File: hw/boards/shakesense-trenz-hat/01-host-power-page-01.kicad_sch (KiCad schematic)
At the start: 9 parts, among them J1 Raspberry Pi 40-pin, U1 24LC32A

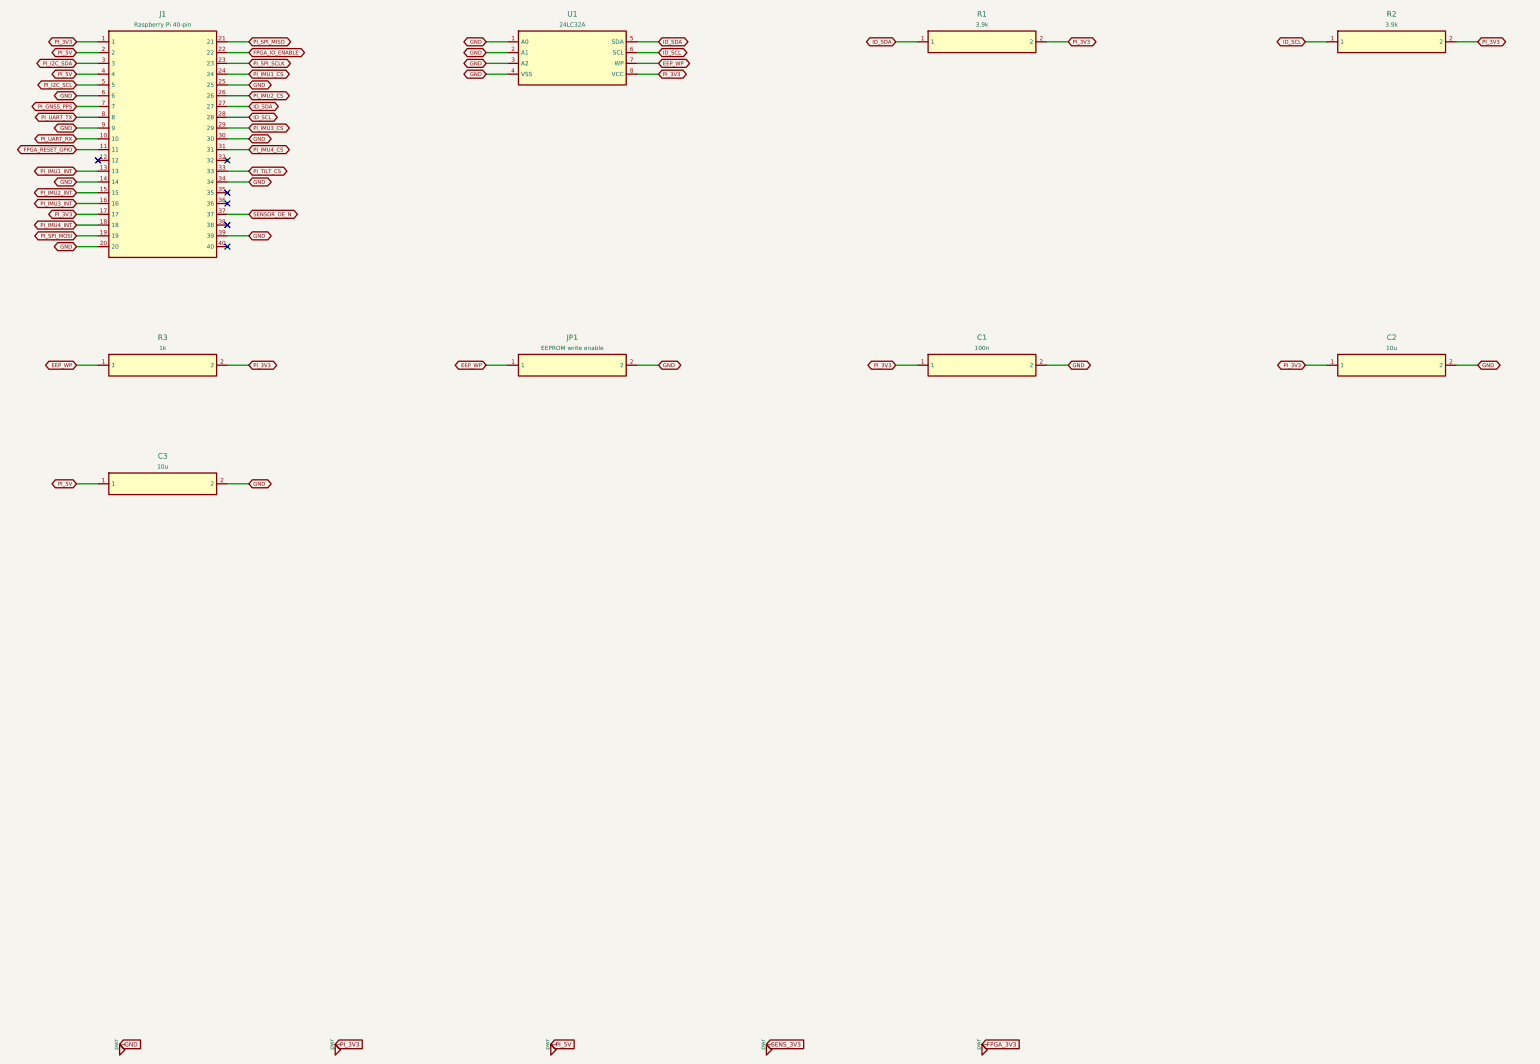
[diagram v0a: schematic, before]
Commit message: Expose Trenz GPIOs on the Pi-outline HDI sensor HAT
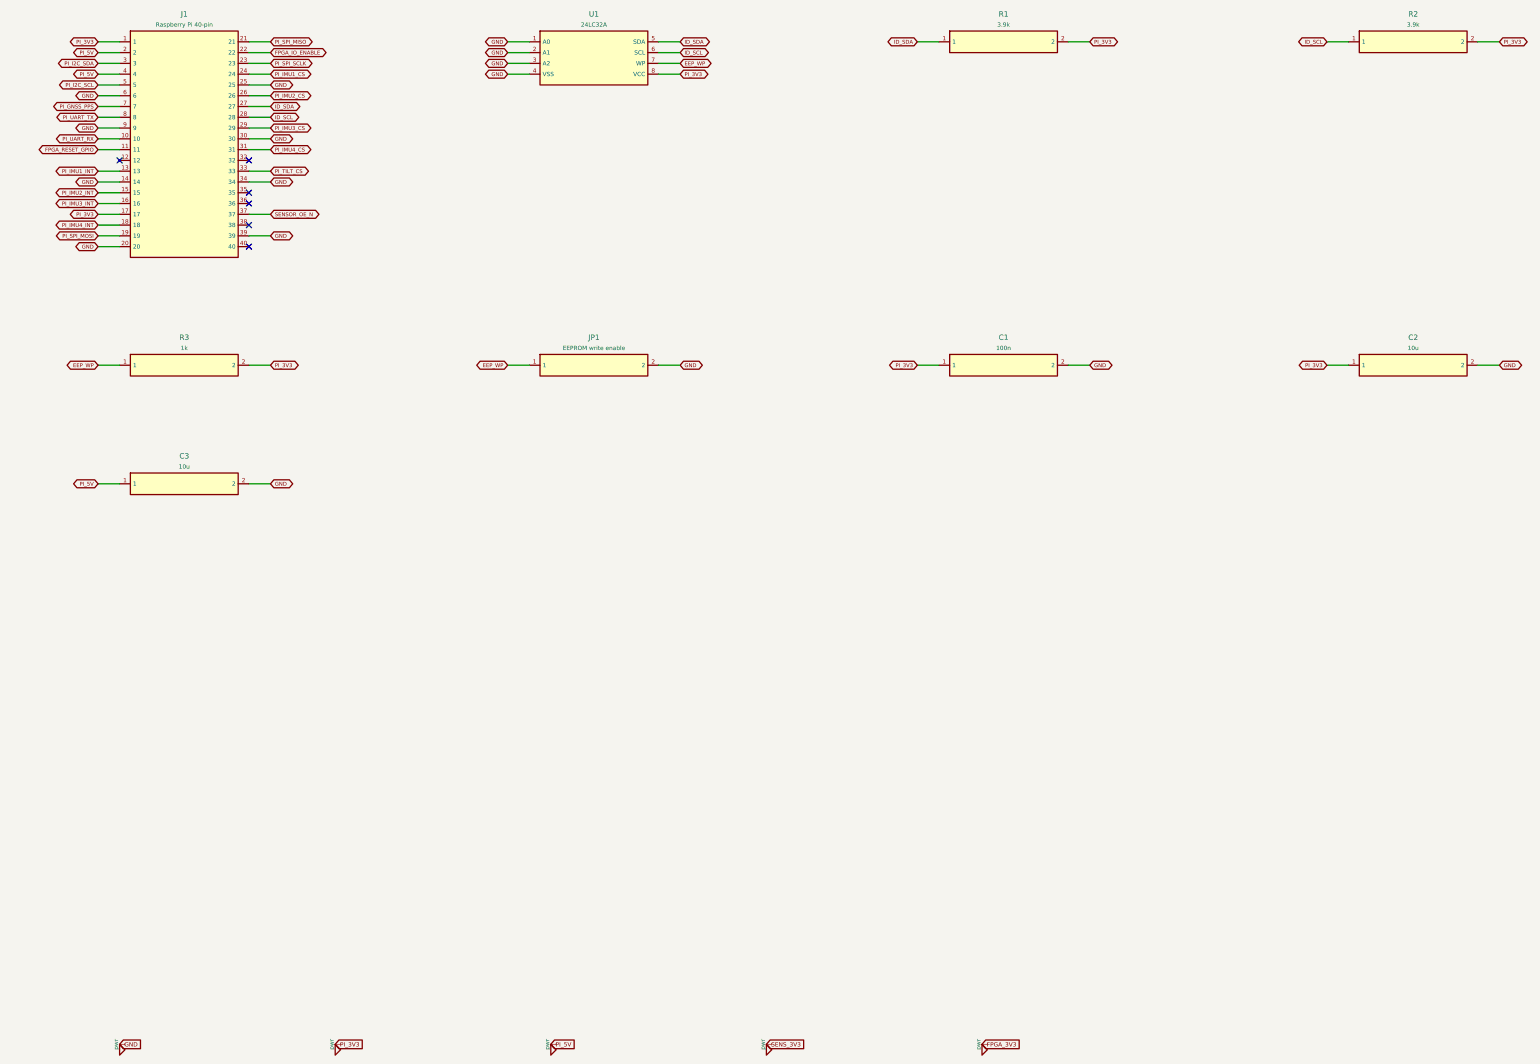
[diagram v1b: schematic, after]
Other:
- title: shakesense-trenz-hat / 01-host-power-page-01 -> ShakeSense T1 / 01-host-power-page-01
- moved on the sheet: C1, C2, C3, J1, JP1, R1, R2, R3, U1

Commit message: Replace T1 GNSS with single Racotech geophone input
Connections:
- net PI_GNSS_PPS renamed PI_GEO_DRDY_N
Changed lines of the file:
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@@
-(kicad_sch (version 20230121) (generator eeschema) (paper "A3") (title_block (title "ShakeSense T1 / 01-host-power-page-01") (date "2026-09-24") (rev "T1-GPIO"))
+(kicad_sch (version 20230121) (generator eeschema) (paper "A3") (title_block (title "ShakeSense T1 / 01-host-power-page-01") (date "2026-09-24") (rev "T1-GEO"))
 (symbol (lib_id "ShakeSense:Part_J1") (at 50.8 62.230000000000004 0) (unit 1) (in_bom yes) (on_board yes) (dnp no)
               (property "Reference" "J1" (at 50.8 31.560000000000002 0) (effects (font (size 1.27 1.27))))
@@
 (global_label "GND" (shape bidirectional) (at 30.48 50.8 180) (effects (font (size 0.9 0.9)) (justify right)))
 (wire (pts (xy 35.56 53.34) (xy 30.48 53.34)) (stroke (width 0) (type default)))
-(global_label "PI_GNSS_PPS" (shape bidirectional) (at 30.48 53.34 180) (effects (font (size 0.9 0.9)) (justify right)))
+(global_label "PI_GEO_DRDY_N" (shape bidirectional) (at 30.48 53.34 180) (effects (font (size 0.9 0.9)) (justify right)))
 (wire (pts (xy 35.56 55.88) (xy 30.48 55.88)) (stroke (width 0) (type default)))
 (global_label "PI_UART_TX" (shape bidirectional) (at 30.48 55.88 180) (effects (font (size 0.9 0.9)) (justify right)))
@@
 (symbol (lib_id "ShakeSense:PWR_FLAG") (at 238.76 274.32 0) (unit 1) (in_bom no) (on_board no) (property "Reference" "#FLG05" (at 238.76 274.32 0) (effects (font (size 1 1)) hide)) (property "Value" "PWR_FLAG" (at 238.76 274.32 0) (effects (font (size 1 1)) hide)) (instances (project "shakesense-trenz-hat" (path "/4ffaaa5d-c728-540d-9f0f-f1cafbdbe36e/94e4fefa-b04f-5cb8-86ce-dd5f9a42bc5a" (reference "#FLG05") (unit 1)))))
 (global_label "FPGA_3V3" (shape input) (at 238.76 274.32 0) (effects (font (size 1.0 1.0)) (justify left)))
+(symbol (lib_id "ShakeSense:PWR_FLAG") (at 289.56 274.32 0) (unit 1) (in_bom no) (on_board no) (property "Reference" "#FLG06" (at 289.56 274.32 0) (effects (font (size 1 1)) hide)) (property "Value" "PWR_FLAG" (at 289.56 274.32 0) (effects (font (size 1 1)) hide)) (instances (project "shakesense-trenz-hat" (path "/4ffaaa5d-c728-540d-9f0f-f1cafbdbe36e/94e4fefa-b04f-5cb8-86ce-dd5f9a42bc5a" (reference "#FLG06") (unit 1)))))
+(global_label "GEO_AVDD" (shape input) (at 289.56 274.32 0) (effects (font (size 1.0 1.0)) (justify left)))
 )

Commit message: Implement internal Pi FPGA link and remove ribbon expansion
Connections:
- net PI_LINK_CS_N: now reaches J1.12
- net PI_LINK_DQ3: now reaches J1.32
- net PI_LINK_DQ1: now reaches J1.35
- net PI_LINK_DQ2: now reaches J1.36
- net PI_LINK_DQ0: now reaches J1.38
- net PI_LINK_SCLK: now reaches J1.40
- no-connect marks 6 -> 0
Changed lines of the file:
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@@
 (wire (pts (xy 35.56 63.5) (xy 30.48 63.5)) (stroke (width 0) (type default)))
 (global_label "FPGA_RESET_GPIO" (shape bidirectional) (at 30.48 63.5 180) (effects (font (size 0.9 0.9)) (justify right)))
-(no_connect (at 35.56 66.04))
+(wire (pts (xy 35.56 66.04) (xy 30.48 66.04)) (stroke (width 0) (type default)))
+(global_label "PI_LINK_CS_N" (shape bidirectional) (at 30.48 66.04 180) (effects (font (size 0.9 0.9)) (justify right)))
 (wire (pts (xy 35.56 68.58) (xy 30.48 68.58)) (stroke (width 0) (type default)))
 (global_label "PI_IMU1_INT" (shape bidirectional) (at 30.48 68.58 180) (effects (font (size 0.9 0.9)) (justify right)))
@@
 (wire (pts (xy 66.04 63.5) (xy 71.12 63.5)) (stroke (width 0) (type default)))
 (global_label "PI_IMU4_CS" (shape bidirectional) (at 71.12 63.5 0) (effects (font (size 0.9 0.9)) (justify left)))
-(no_connect (at 66.04 66.04))
+(wire (pts (xy 66.04 66.04) (xy 71.12 66.04)) (stroke (width 0) (type default)))
+(global_label "PI_LINK_DQ3" (shape bidirectional) (at 71.12 66.04 0) (effects (font (size 0.9 0.9)) (justify left)))
 (wire (pts (xy 66.04 68.58) (xy 71.12 68.58)) (stroke (width 0) (type default)))
 (global_label "PI_TILT_CS" (shape bidirectional) (at 71.12 68.58 0) (effects (font (size 0.9 0.9)) (justify left)))
 (wire (pts (xy 66.04 71.12) (xy 71.12 71.12)) (stroke (width 0) (type default)))
 (global_label "GND" (shape bidirectional) (at 71.12 71.12 0) (effects (font (size 0.9 0.9)) (justify left)))
-(no_connect (at 66.04 73.66))
-(no_connect (at 66.04 76.2))
+(wire (pts (xy 66.04 73.66) (xy 71.12 73.66)) (stroke (width 0) (type default)))
+(global_label "PI_LINK_DQ1" (shape bidirectional) (at 71.12 73.66 0) (effects (font (size 0.9 0.9)) (justify left)))
+(wire (pts (xy 66.04 76.2) (xy 71.12 76.2)) (stroke (width 0) (type default)))
+(global_label "PI_LINK_DQ2" (shape bidirectional) (at 71.12 76.2 0) (effects (font (size 0.9 0.9)) (justify left)))
 (wire (pts (xy 66.04 78.74) (xy 71.12 78.74)) (stroke (width 0) (type default)))
 (global_label "SENSOR_OE_N" (shape bidirectional) (at 71.12 78.74 0) (effects (font (size 0.9 0.9)) (justify left)))
-(no_connect (at 66.04 81.28))
+(wire (pts (xy 66.04 81.28) (xy 71.12 81.28)) (stroke (width 0) (type default)))
+(global_label "PI_LINK_DQ0" (shape bidirectional) (at 71.12 81.28 0) (effects (font (size 0.9 0.9)) (justify left)))
 (wire (pts (xy 66.04 83.82) (xy 71.12 83.82)) (stroke (width 0) (type default)))
 (global_label "GND" (shape bidirectional) (at 71.12 83.82 0) (effects (font (size 0.9 0.9)) (justify left)))
-(no_connect (at 66.04 86.36))
+(wire (pts (xy 66.04 86.36) (xy 71.12 86.36)) (stroke (width 0) (type default)))
+(global_label "PI_LINK_SCLK" (shape bidirectional) (at 71.12 86.36 0) (effects (font (size 0.9 0.9)) (justify left)))
 (symbol (lib_id "ShakeSense:Part_U1") (at 147.32 41.910000000000004 0) (unit 1) (in_bom yes) (on_board yes) (dnp no)
               (property "Reference" "U1" (at 147.32 31.560000000000002 0) (effects (font (size 1.27 1.27))))
